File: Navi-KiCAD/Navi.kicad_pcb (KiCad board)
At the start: 4 copper layers, 50.8 x 40 mm, 216 parts, among them J1 0734120110, J2 0734120110, J3 0734120110, J4 473460001, J5 AXK5S80047YG, J6 AXK5S80047YG, Q1 IRLML5203TRPBF, Q2 IRLML5203TRPBF, U1 LP55231SQE/NOPB, U10 TPS54232DR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

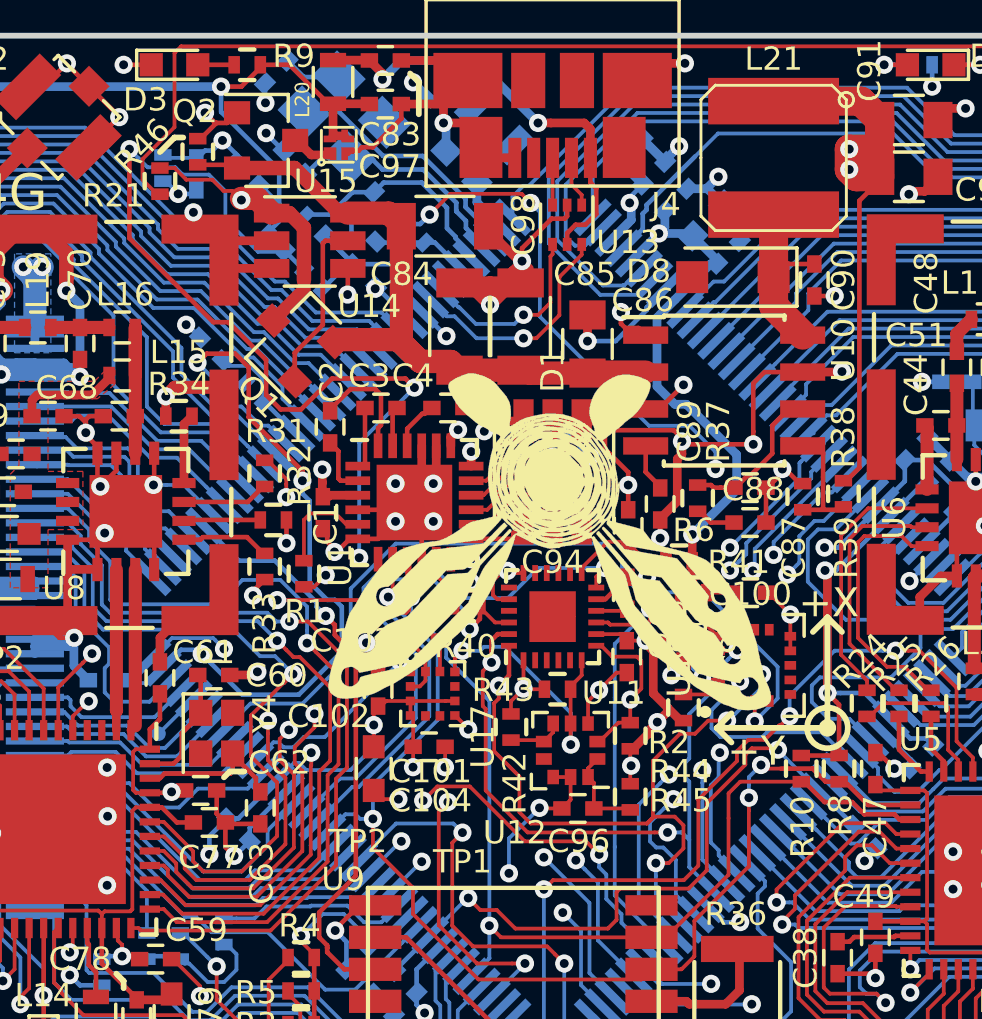
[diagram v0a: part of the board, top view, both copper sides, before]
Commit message: Cleaned up 3D models and rebuilt outputs.
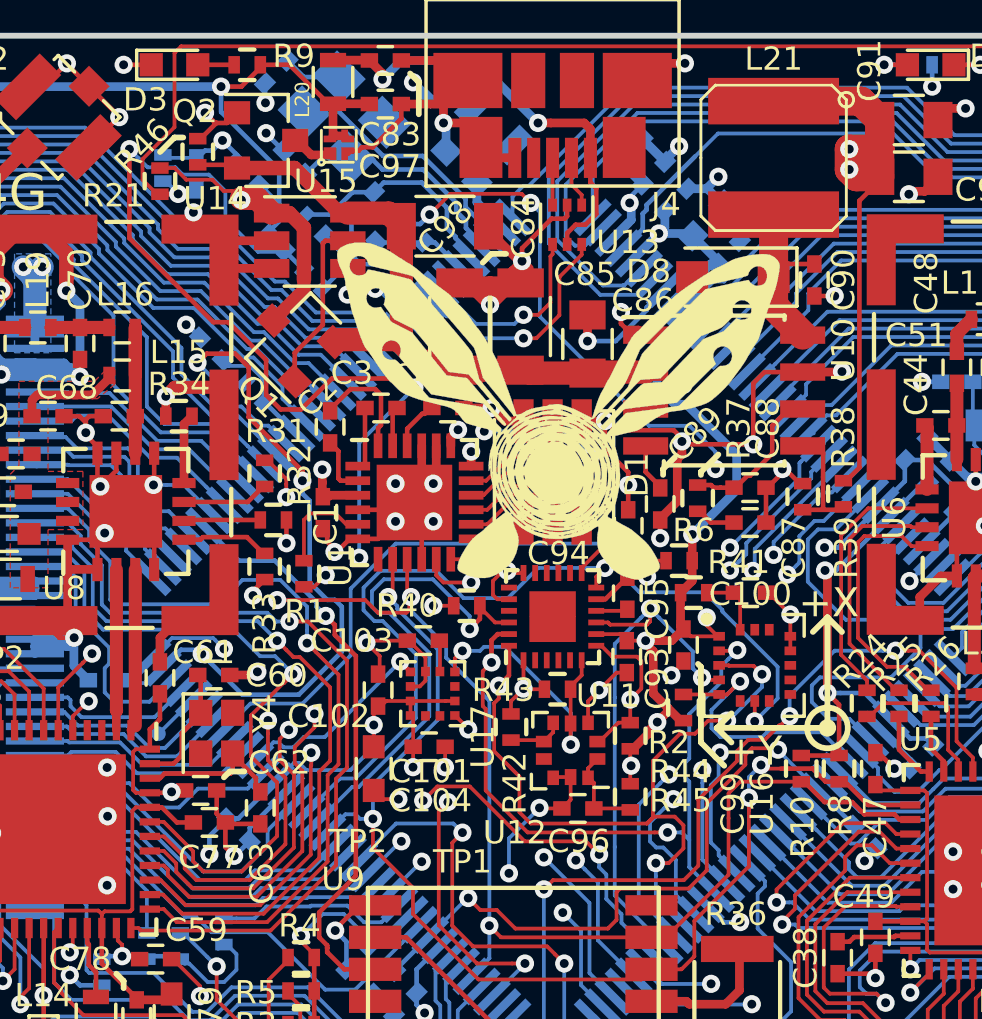
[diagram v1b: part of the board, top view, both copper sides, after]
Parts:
- J4: value 473460001 -> 0473460001
- moved U3 3.57 mm to (74.7, 98.4), turned to 350 degrees
